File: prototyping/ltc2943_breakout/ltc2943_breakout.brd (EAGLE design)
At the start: 17.8 x 15.2 mm, 12 parts, among them U1 LTC2943

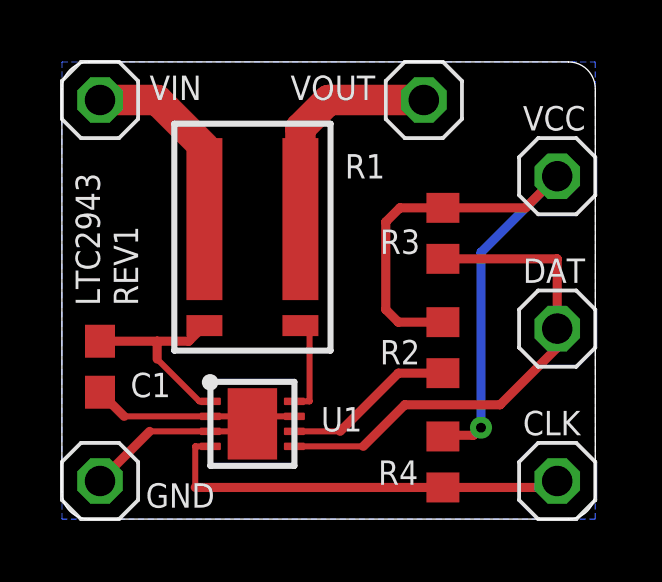
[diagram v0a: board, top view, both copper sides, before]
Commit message: Updated ltc2943 breakout board.
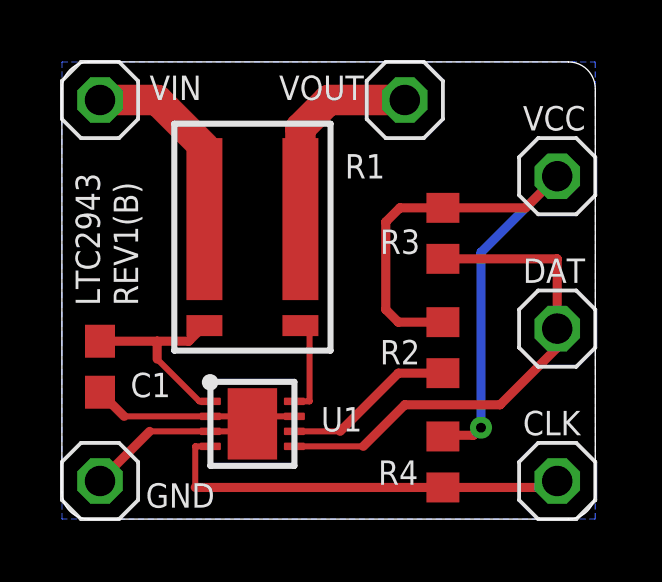
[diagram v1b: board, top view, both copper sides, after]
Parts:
- moved JP2 0.64 mm to (12.7, 15.2)
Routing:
- net VOUT: track 7.53 -> 6.90 mm
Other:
- board text added: "REV1(B)"
- board text removed: "REV1"
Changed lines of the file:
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@@
 <setting verticaltext="up"/>
 </settings>
-<grid distance="25" unitdist="mil" unit="mil" style="lines" multiple="1" display="yes" altdistance="5" altunitdist="mil" altunit="mil"/>
+<grid distance="100" unitdist="mil" unit="mil" style="lines" multiple="1" display="yes" altdistance="5" altunitdist="mil" altunit="mil"/>
 <layers>
 <layer number="1" name="Top" color="4" fill="1" visible="yes" active="yes"/>
@@
 <wire x1="2.168025" y1="16.51" x2="1.27" y2="15.611975" width="0" layer="20" curve="90"/>
 <text x="4.191" y="15.24" size="0.8128" layer="21" font="vector" ratio="10">VIN</text>
-<text x="8.89" y="15.24" size="0.8128" layer="21" font="vector" ratio="10">VOUT</text>
+<text x="8.509" y="15.24" size="0.8128" layer="21" font="vector" ratio="10">VOUT</text>
 <text x="16.637" y="14.224" size="0.8128" layer="21" font="vector" ratio="10">VCC</text>
 <text x="16.637" y="9.144" size="0.8128" layer="21" font="vector" ratio="10">DAT</text>
@@
 <text x="4.064" y="1.651" size="0.8128" layer="21" font="vector" ratio="10">GND</text>
 <text x="2.54" y="8.382" size="0.8128" layer="21" font="vector" ratio="10" rot="R90">LTC2943</text>
-<text x="3.81" y="8.382" size="0.8128" layer="21" font="vector" ratio="10" rot="R90">REV1</text>
+<text x="3.81" y="8.382" size="0.8128" layer="21" font="vector" ratio="10" rot="R90">REV1(B)</text>
 </plain>
 <attributes>
@@
 <attribute name="VALUE" x="1.27" y="12.065" size="1.27" layer="27"/>
 </element>
-<element name="JP2" library="ltc2943_breakout" package="1X01" value="" x="13.335" y="15.24" smashed="yes">
-<attribute name="VALUE" x="12.065" y="12.065" size="1.27" layer="27"/>
+<element name="JP2" library="ltc2943_breakout" package="1X01" value="" x="12.7" y="15.24" smashed="yes">
+<attribute name="VALUE" x="11.43" y="12.065" size="1.27" layer="27"/>
 </element>
 <element name="JP4" library="ltc2943_breakout" package="1X01" value="" x="17.78" y="7.62" smashed="yes">
@@
 <contactref element="R1" pad="I1"/>
 <contactref element="JP2" pad="1"/>
-<wire x1="13.335" y1="15.24" x2="10.16" y2="15.24" width="1.016" layer="1"/>
+<wire x1="12.7" y1="15.24" x2="10.16" y2="15.24" width="1.016" layer="1"/>
 <wire x1="10.16" y1="15.24" x2="9.22" y2="14.3" width="1.016" layer="1"/>
 <wire x1="9.22" y1="14.3" x2="9.22" y2="11.27" width="1.016" layer="1"/>
